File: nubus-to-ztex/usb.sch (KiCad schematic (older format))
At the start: 13 parts, among them J6 105017-0001 (USB micro-B), U10 SN65220DBV, U11 TPS2051CDBV

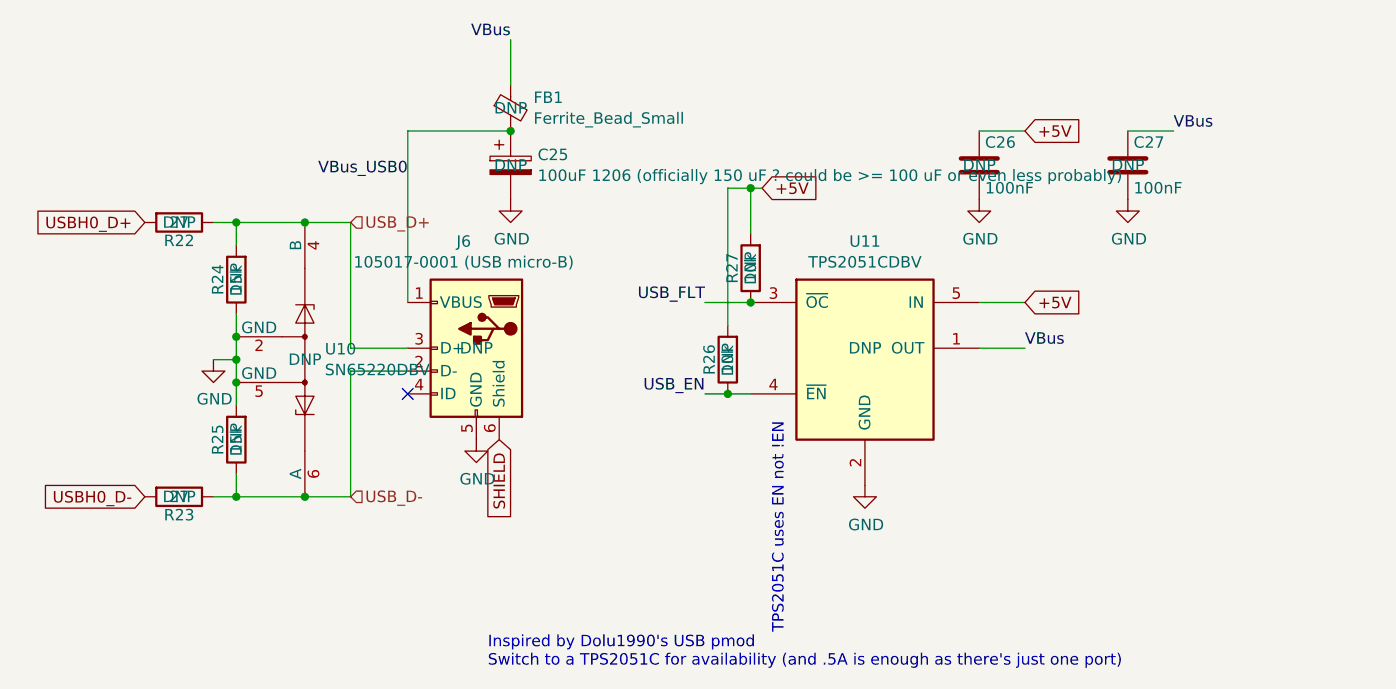
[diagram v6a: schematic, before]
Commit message: even more JLCPCB BoM optimization
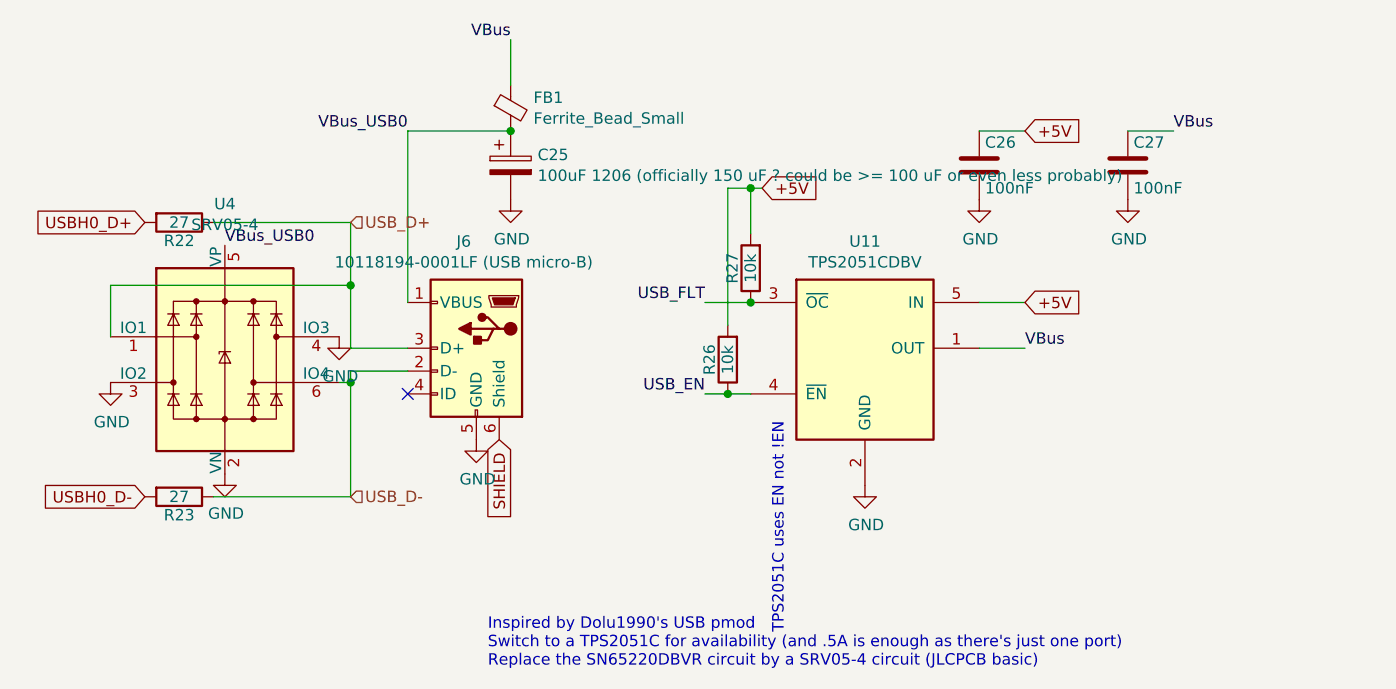
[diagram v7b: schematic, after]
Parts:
- removed R24, R25: 15k, Resistor_SMD:R_0603_1608Metric, symbol Device:R
- removed U10: SN65220DBV, Package_TO_SOT_SMD:SOT-23-6, symbol Power_Protection:SN65220
- added U4: SRV05-4, Package_TO_SOT_SMD:SOT-23-6, symbol Power_Protection:SRV05-4
- C25: DNP DNP -> (none); MPN JMK316ABJ107ML-T -> CL31A107MQHNNNE; MPN-ALT2 (none) -> JMK316ABJ107ML-T; URL https://www.lcsc.com/product-detail/Multilayer-Ceramic-Capacitors-MLCC-SMD-SMT_Taiyo-Yuden-JMK316ABJ107ML-T_C268006.html -> https://www.lcsc.com/product-detail/Multilayer-Ceramic-Capacitors-MLCC-SMD-SMT_Samsung-Electro-Mechanics-CL31A107MQHNNNE_C15008.html; URL-ALT2 (none) -> https://www.lcsc.com/product-detail/Multilayer-Ceramic-Capa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
- C26, C27: DNP DNP -> (none); Mouser 603-CC603KRX7R8BB104 -> (none)
- FB1: DNP DNP -> (none); MPN PZ2012U221-2R0TF -> BLM21PG221SN1D; MPN-ALT2 (none) -> PZ2012U221-2R0TF; URL https://www.lcsc.com/product-detail/Ferrite-Beads_Sunlord-P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 -> https://www.lcsc.com/product-detail/Ferrite-Beads_Murata-El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; URL-ALT2 (none) -> https://www.lcsc.com/product-detail/Ferrite-Beads_Sunlord-P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
- J6: value 105017-0001 (USB micro-B) -> 10118194-0001LF (USB micro-B); footprint Connector_USB:USB_Micro-B_Molex-105017-0001 -> Connector_USB:USB_Micro-B_Amphenol_10118194_Horizontal; DNP DNP -> (none); MPN 105017-0001 -> 10118194-0001LF; Manufacturer Molex -> (none); URL https://www.lcsc.com/product-detail/USB-Connectors_MOLEX-10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 -> https://www.lcsc.com/product-detail/USB-Connectors_Amphenol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; URL-ALT https://www.mouser.fr/ProductDetail/Molex/105017-0001?qs=hl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 -> (none)
- R22, R23, R26, R27, U11: DNP DNP -> (none)
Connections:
- net GND: now also U4.2 (VN), U4.3 (IO2), U4.4 (IO3)
- net USB_D+: now also U4.1 (IO1)
- net USB_D-: now also U4.6 (IO4)
- net VBus_USB0: now also U4.5 (VP)
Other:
- note added: "Inspired by Dolu1990's USB pmod\nSwitch to a TPS2051C for availability (and .5A is enough as there's just one port)\nReplace the SN65220DBVR circuit by a SRV05-4 circuit (JLCPCB basic)"
- note removed: "Inspired by Dolu1990's USB pmod\nSwitch to a TPS2051C for availability (and .5A is enough as there's just one port)\n"
